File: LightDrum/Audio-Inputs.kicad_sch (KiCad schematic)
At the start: 37 parts, among them J201 XLR3, J202 SJ-43515RS-SMT-TR, Q201 NX6008NBKWX, Q202 NX6008NBKWX, U201 MCP3561R, U202 AZV321, U203 MCP3561R, U204 AZV321, U205 AZV321

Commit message: Lock REV8 Layout and send to PCB MNF
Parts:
- R202, R207: footprint Resistor_SMD:R_0805_2012Metric -> Resistor_SMD:R_0603_1608Metric
- R210, R217: value 1K -> 10K
- RV201, RV202: footprint Potentiometer_SMD:Potentiometer_Bourns_3214W_Vertical -> Daxxn_Switches:Bourns_3214W_Vertical
- U201, U203: footprint Package_DFN_QFN:QFN-20-1EP_3x3mm_P0.4mm_EP1.65x1.65mm -> Daxxn_Packages:QFN-20-1EP_3x3mm_P0.4mm_EP1.65x1.65mm
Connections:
- net AGND: now also RV202.1; no longer RV202.3
- net at C206.1, R205.1, U204.1 (IN+): now also RV202.3; no longer RV202.1
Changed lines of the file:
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@@
       (effects (font (size 1.27 1.27)) (justify right))
     )
-    (property "Footprint" "Potentiometer_SMD:Potentiometer_Bourns_3214W_Vertical" (id 2) (at 67.31 53.34 0)
+    (property "Footprint" "Daxxn_Switches:Bourns_3214W_Vertical" (id 2) (at 67.31 53.34 0)
       (effects (font (size 1.27 1.27)) hide)
     )
@@
       (effects (font (size 1.27 1.27)) (justify right))
     )
-    (property "Footprint" "Resistor_SMD:R_0805_2012Metric" (id 2) (at 149.86 48.26 0)
+    (property "Footprint" "Resistor_SMD:R_0603_1608Metric" (id 2) (at 149.86 48.26 0)
       (effects (font (size 1.27 1.27)) hide)
     )
@@
       (effects (font (size 1.27 1.27)) (justify right))
     )
-    (property "Footprint" "Resistor_SMD:R_0805_2012Metric" (id 2) (at 148.59 100.33 0)
+    (property "Footprint" "Resistor_SMD:R_0603_1608Metric" (id 2) (at 148.59 100.33 0)
       (effects (font (size 1.27 1.27)) hide)
     )
@@
     (in_bom yes) (on_board yes)
     (property "Reference" "R210" (id 0) (at 44.45 143.002 90))
-    (property "Value" "1K" (id 1) (at 44.45 144.78 90))
+    (property "Value" "10K" (id 1) (at 44.45 144.78 90))
     (property "Footprint" "Resistor_SMD:R_0805_2012Metric" (id 2) (at 44.45 140.97 0)
       (effects (font (size 1.27 1.27)) hide)
@@
       (effects (font (size 1.27 1.27)) (justify left))
     )
-    (property "Footprint" "Package_DFN_QFN:QFN-20-1EP_3x3mm_P0.4mm_EP1.65x1.65mm" (id 2) (at 116.84 21.59 0)
+    (property "Footprint" "Daxxn_Packages:QFN-20-1EP_3x3mm_P0.4mm_EP1.65x1.65mm" (id 2) (at 116.84 21.59 0)
       (effects (font (size 1.27 1.27)) hide)
     )
@@
       (effects (font (size 1.27 1.27)) hide)
     )
-    (property "Datasheet" "https://optoelectronics.liteon.com/upload/download/DS22-2010-0048/LTST-S321TBKT.pdf" (id 3) (at 29.21 154.94 90)
+    (property "Datasheet" "~" (id 3) (at 29.21 154.94 90)
       (effects (font (size 1.27 1.27)) hide)
     )
@@
     (pin "1")
   )
-  (symbol (lib_id "Device:R_Potentiometer_Small") (at 68.58 104.14 0) (unit 1)
-    (in_bom yes) (on_board yes)
-    (property "Reference" "RV202" (id 0) (at 67.564 103.378 0)
-      (effects (font (size 1.27 1.27)) (justify right))
-    )
-    (property "Value" "30K" (id 1) (at 67.564 105.156 0)
-      (effects (font (size 1.27 1.27)) (justify right))
-    )
-    (property "Footprint" "Potentiometer_SMD:Potentiometer_Bourns_3214W_Vertical" (id 2) (at 68.58 104.14 0)
+  (symbol (lib_id "Device:R_Potentiometer_Small") (at 68.58 104.14 0) (mirror x) (unit 1)
+    (in_bom yes) (on_board yes)
+    (property "Reference" "RV202" (id 0) (at 67.564 104.902 0)
+      (effects (font (size 1.27 1.27)) (justify right))
+    )
+    (property "Value" "30K" (id 1) (at 67.564 103.124 0)
+      (effects (font (size 1.27 1.27)) (justify right))
+    )
+    (property "Footprint" "Daxxn_Switches:Bourns_3214W_Vertical" (id 2) (at 68.58 104.14 0)
       (effects (font (size 1.27 1.27)) hide)
     )
@@
       (effects (font (size 1.27 1.27)) hide)
     )
-    (property "Datasheet" "https://optoelectronics.liteon.com/upload/download/DS22-2010-0048/LTST-S321TBKT.pdf" (id 3) (at 29.21 134.62 90)
+    (property "Datasheet" "~" (id 3) (at 29.21 134.62 90)
       (effects (font (size 1.27 1.27)) hide)
     )
@@
     (in_bom yes) (on_board yes)
     (property "Reference" "R217" (id 0) (at 44.45 163.322 90))
-    (property "Value" "1K" (id 1) (at 44.45 165.1 90))
+    (property "Value" "10K" (id 1) (at 44.45 165.1 90))
     (property "Footprint" "Resistor_SMD:R_0805_2012Metric" (id 2) (at 44.45 161.29 0)
       (effects (font (size 1.27 1.27)) hide)
@@
       (effects (font (size 1.27 1.27)) (justify left))
     )
-    (property "Footprint" "Package_DFN_QFN:QFN-20-1EP_3x3mm_P0.4mm_EP1.65x1.65mm" (id 2) (at 116.84 73.66 0)
-      (effects (font (size 1.27 1.27)) hide)
-    )
+    (property "Footprint" "Daxxn_Packages:QFN-20-1EP_3x3mm_P0.4mm_EP1.65x1.65mm" (id 2) (at 116.84 73.66 0)
+      (effects (font (size 1.27 1.27)) hide)
+    )

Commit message: Replace old MCU W/ STM32F412
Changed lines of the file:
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@@
     (stroke (width 0) (type default) (color 0 0 0 0))
   )
-  (wire (pts (xy 59.69 99.06) (xy 59.69 100.33))
+  (wire (pts (xy 57.15 99.06) (xy 57.15 100.33))
     (stroke (width 0) (type default) (color 0 0 0 0))
   )
@@
     (stroke (width 0) (type default) (color 0 0 0 0))
   )
-  (wire (pts (xy 59.69 100.33) (xy 60.96 100.33))
+  (wire (pts (xy 57.15 100.33) (xy 60.96 100.33))
     (stroke (width 0) (type default) (color 0 0 0 0))
   )
@@
   (symbol (lib_id "Device:C_Small") (at 134.62 81.28 0) (unit 1)
     (in_bom yes) (on_board yes)
-    (property "Reference" "C205" (id 0) (at 134.874 79.502 0)
-      (effects (font (size 1.27 1.27)) (justify left))
-    )
-    (property "Value" "100nF" (id 1) (at 134.874 83.312 0)
+    (property "Reference" "C205" (id 0) (at 134.62 79.756 0)
+      (effects (font (size 1.27 1.27)) (justify left))
+    )
+    (property "Value" "100nF" (id 1) (at 134.62 83.058 0)
       (effects (font (size 1.27 1.27)) (justify left))
     )
@@
   (symbol (lib_id "Device:C_Small") (at 71.12 140.97 0) (unit 1)
     (in_bom yes) (on_board yes)
-    (property "Reference" "C207" (id 0) (at 71.374 139.192 0)
-      (effects (font (size 1.27 1.27)) (justify left))
-    )
-    (property "Value" "100nF" (id 1) (at 71.374 143.002 0)
+    (property "Reference" "C207" (id 0) (at 71.12 139.446 0)
+      (effects (font (size 1.27 1.27)) (justify left))
+    )
+    (property "Value" "100nF" (id 1) (at 71.12 142.748 0)
       (effects (font (size 1.27 1.27)) (justify left))
     )
@@
   (symbol (lib_id "Device:R_Small_US") (at 63.5 100.33 270) (mirror x) (unit 1)
     (in_bom yes) (on_board yes)
-    (property "Reference" "R205" (id 0) (at 64.008 99.568 0)
-      (effects (font (size 1.27 1.27)) (justify left))
-    )
-    (property "Value" "1K" (id 1) (at 62.484 99.568 0)
-      (effects (font (size 1.27 1.27)) (justify left))
-    )
+    (property "Reference" "R205" (id 0) (at 63.5 96.52 90))
+    (property "Value" "1K" (id 1) (at 63.5 98.298 90))
     (property "Footprint" "Resistor_SMD:R_0603_1608Metric" (id 2) (at 63.5 100.33 0)
       (effects (font (size 1.27 1.27)) hide)
@@
   (symbol (lib_id "Device:R_Small_US") (at 85.09 142.24 180) (unit 1)
     (in_bom yes) (on_board yes)
-    (property "Reference" "R215" (id 0) (at 82.296 140.716 90)
-      (effects (font (size 1.27 1.27)) (justify right))
-    )
-    (property "Value" "2.4K" (id 1) (at 84.074 140.716 90)
-      (effects (font (size 1.27 1.27)) (justify right))
+    (property "Reference" "R215" (id 0) (at 83.82 141.478 0)
+      (effects (font (size 1.27 1.27)) (justify left))
+    )
+    (property "Value" "2.4K" (id 1) (at 83.82 143.256 0)
+      (effects (font (size 1.27 1.27)) (justify left))
     )
     (property "Footprint" "Resistor_SMD:R_0805_2012Metric" (id 2) (at 85.09 142.24 0)
@@
   (symbol (lib_id "Device:R_Small_US") (at 85.09 149.86 180) (unit 1)
     (in_bom yes) (on_board yes)
-    (property "Reference" "R216" (id 0) (at 86.36 148.336 90)
-      (effects (font (size 1.27 1.27)) (justify right))
-    )
-    (property "Value" "7.5K" (id 1) (at 88.138 148.336 90)
-      (effects (font (size 1.27 1.27)) (justify right))
+    (property "Reference" "R216" (id 0) (at 83.82 149.352 0)
+      (effects (font (size 1.27 1.27)) (justify left))
+    )
+    (property "Value" "7.5K" (id 1) (at 83.82 151.13 0)
+      (effects (font (size 1.27 1.27)) (justify left))
     )
     (property "Footprint" "Resistor_SMD:R_0805_2012Metric" (id 2) (at 85.09 149.86 0)
@@
     (pin "2")
   )
-  (symbol (lib_id "power:VDDA") (at 59.69 99.06 0) (unit 1)
-    (in_bom yes) (on_board yes)
-    (property "Reference" "#PWR0218" (id 0) (at 59.69 102.87 0)
-      (effects (font (size 1.27 1.27)) hide)
-    )
-    (property "Value" "VDDA" (id 1) (at 59.69 95.25 0))
-    (property "Footprint" "" (id 2) (at 59.69 99.06 0)
-      (effects (font (size 1.27 1.27)) hide)
-    )
-    (property "Datasheet" "" (id 3) (at 59.69 99.06 0)
-      (effects (font (size 1.27 1.27)) hide)
-    )
+  (symbol (lib_id "power:VDDA") (at 57.15 99.06 0) (unit 1)
+    (in_bom yes) (on_board yes)
+    (property "Reference" "#PWR0218" (id 0) (at 57.15 102.87 0)
+      (effects (font (size 1.27 1.27)) hide)
+    )
+    (property "Value" "VDDA" (id 1) (at 57.15 95.25 0))
+    (property "Footprint" "" (id 2) (at 57.15 99.06 0)
+      (effects (font (size 1.27 1.27)) hide)
+    )
+    (property "Datasheet" "" (id 3) (at 57.15 99.06 0)
+      (effects (font (size 1.27 1.27)) hide)
+    )

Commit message: interface layout completed - REV6
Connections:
- net HP-REF: now reaches C206.1, R205.1, RV202.3, U204.1 (IN+)
- net XLR-REF: now reaches C203.1, R201.1, RV201.3, U202.1 (IN+)
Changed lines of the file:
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@@
+    (stroke (width 0) (type default) (color 0 0 0 0))
+  )
+  (wire (pts (xy 67.31 45.72) (xy 67.31 48.26))
     (stroke (width 0) (type default) (color 0 0 0 0))
   )
@@
     (stroke (width 0) (type default) (color 0 0 0 0))
   )
+  (wire (pts (xy 68.58 97.79) (xy 68.58 100.33))
+    (stroke (width 0) (type default) (color 0 0 0 0))
+  )
   (polyline (pts (xy 170.18 17.78) (xy 170.18 69.85))
     (stroke (width 0) (type solid) (color 0 0 0 0))
@@
     (stroke (width 0) (type default) (color 0 0 0 0))
   )
+  (wire (pts (xy 73.66 97.79) (xy 68.58 97.79))
+    (stroke (width 0) (type default) (color 0 0 0 0))
+  )
   (wire (pts (xy 48.26 134.62) (xy 44.45 134.62))
     (stroke (width 0) (type default) (color 0 0 0 0))
@@
   )
   (wire (pts (xy 68.58 113.03) (xy 68.58 107.95))
+    (stroke (width 0) (type default) (color 0 0 0 0))
+  )
+  (wire (pts (xy 72.39 45.72) (xy 67.31 45.72))
     (stroke (width 0) (type default) (color 0 0 0 0))
   )
@@
     )
   )
+  (global_label "HP-REF" (shape input) (at 73.66 97.79 0) (fields_autoplaced)
+    (effects (font (size 1 1)) (justify left))
+    (property "Intersheet References" "${INTERSHEET_REFS}" (id 0) (at 81.6076 97.7275 0)
+      (effects (font (size 1 1)) (justify left) hide)
+    )
+  )
   (global_label "SPI-CIPO" (shape input) (at 133.35 96.52 0) (fields_autoplaced)
     (effects (font (size 1.1 1.1) (thickness 0.254) bold) (justify left))
@@
     )
   )
+  (global_label "XLR-REF" (shape input) (at 72.39 45.72 0) (fields_autoplaced)
+    (effects (font (size 1 1)) (justify left))
+    (property "Intersheet References" "${INTERSHEET_REFS}" (id 0) (at 81.0519 45.6575 0)
+      (effects (font (size 1 1)) (justify left) hide)
+    )
+  )

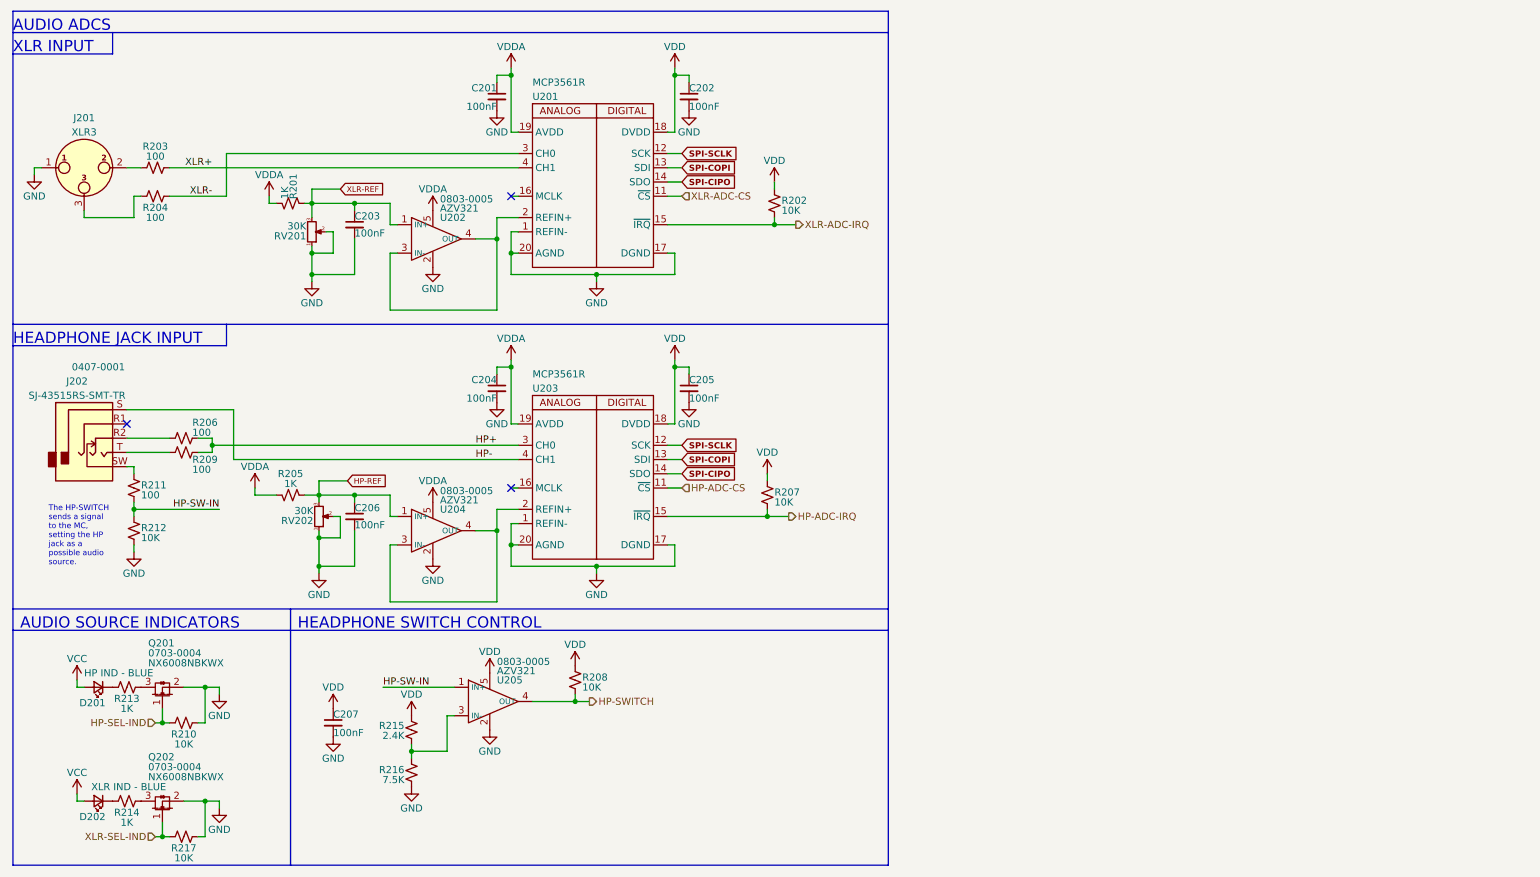
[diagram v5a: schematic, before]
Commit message: Add main page to sch and xlr audio input diff-amp
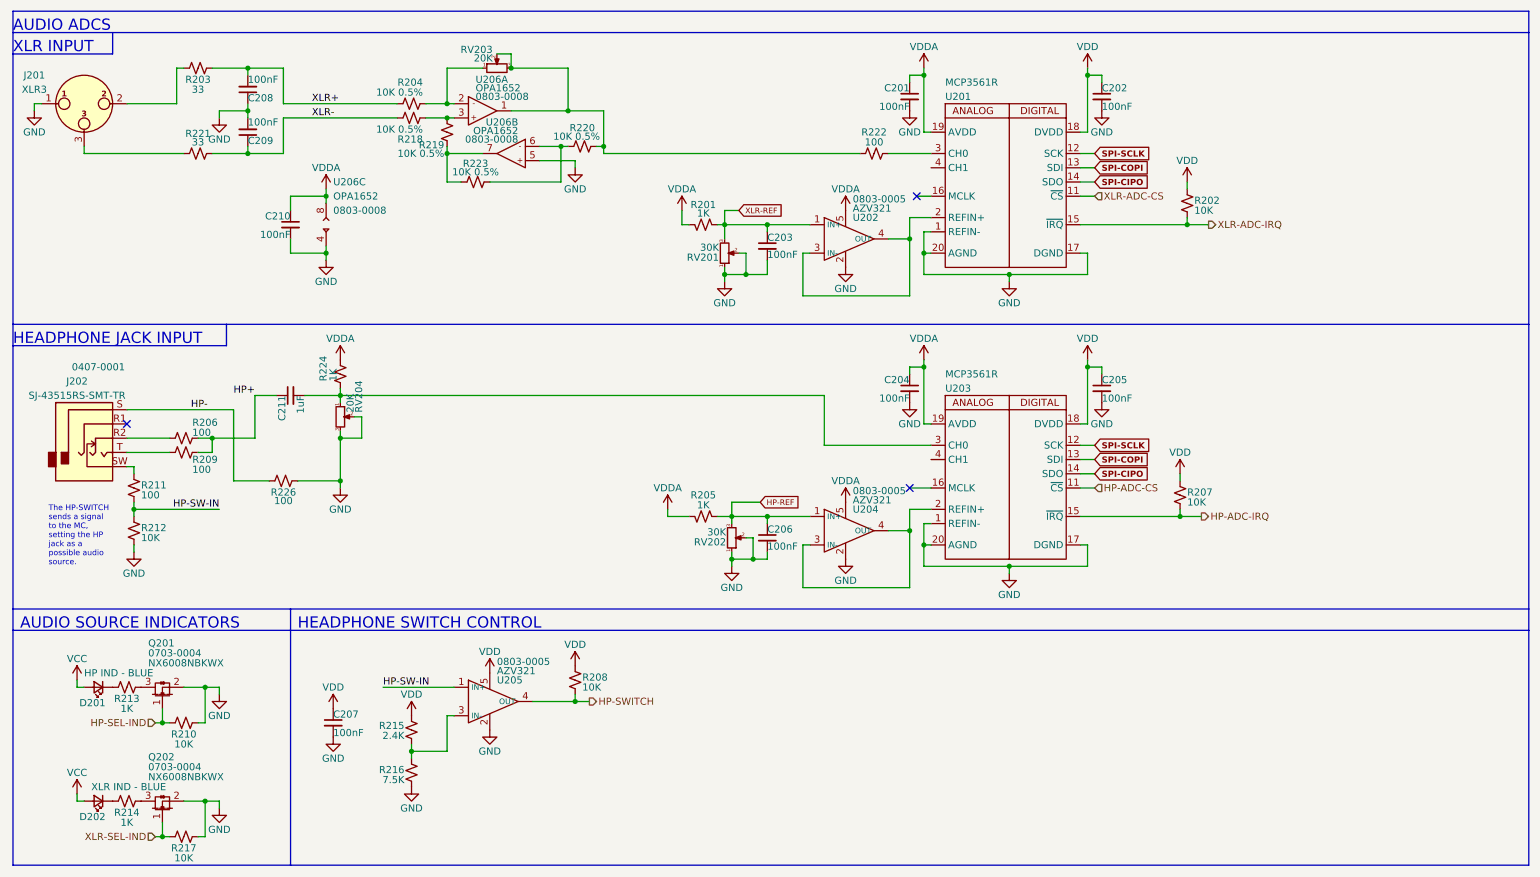
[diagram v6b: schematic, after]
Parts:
- added C208, C209, C210: 100nF, Capacitor_SMD:C_0603_1608Metric, symbol Device:C_Small
- added C211: 1uF, Capacitor_SMD:C_0805_2012Metric, symbol Device:C_Small
- added R218, R219, R220, R223: 10K 0.5%, Resistor_SMD:R_0603_1608Metric, symbol Device:R_Small_US
- added R221: 33, Resistor_SMD:R_0603_1608Metric, symbol Device:R_Small_US
- added R222: 100, Resistor_SMD:R_0805_2012Metric, symbol Device:R_Small_US
- added R224: 1K, Resistor_SMD:R_0805_2012Metric, symbol Device:R_Small_US
- added R226: 100, Resistor_SMD:R_0603_1608Metric, symbol Device:R_Small_US
- added RV203, RV204: 20K, Potentiometer_SMD:Potentiometer_Bourns_3214W_Vertical, symbol Device:R_Potentiometer_Small
- added U206: OPA1652, Package_SO:VSSOP-8_3.0x3.0mm_P0.65mm, symbol Daxxn_OPAMP:OPA1652
- R203: value 100 -> 33; footprint Resistor_SMD:R_0805_2012Metric -> Resistor_SMD:R_0603_1608Metric
- R204: value 100 -> 10K 0.5%; footprint Resistor_SMD:R_0805_2012Metric -> Resistor_SMD:R_0603_1608Metric
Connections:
- net AGND: now also C208.1, C209.2, C210.2, R226.2, RV204.2, RV204.3, U206.4, U206.5
- net HP+: now also C211.1; no longer U203.3 (CH0)
- net HP-: now also R226.1; no longer U203.4 (CH1)
- net VDDA: now also C210.1, R224.2, U206.8
- net XLR+: now also R204.1, C208.2; no longer U201.4 (CH1)
- net XLR-: now also C209.1, R218.2, R221.2; no longer R204.2, U201.3 (CH0)
- net at J201.3: now also R221.1; no longer R204.1
- new net: C211.2, R224.1, RV204.1, U203.3 (CH0)
- new net: R219.1, R223.1, U206.7
- new net: R220.1, R223.2, U206.6
- new net: R220.2, R222.1, RV203.2, RV203.3, U206.1
- new net: R222.2, U201.3 (CH0)
- new net: R204.2, RV203.1, U206.2
- new net: R218.1, R219.2, U206.3
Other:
- moved on the sheet: C201, C202, C203, C204, C205, C206, J201, R201, R202, R205, R207, RV201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
